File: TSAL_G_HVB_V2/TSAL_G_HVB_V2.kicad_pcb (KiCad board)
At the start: 2 copper layers, 100 x 50 mm, 48 parts, among them J1 Conn_01x03_Pin, J2 Conn_01x02_Pin, J3 Conn_01x02_Pin, J4 Conn_01x02_Pin, Q1 2N7002, Q2 MMBT3904, Q3 PMOS, U1 uA7805, U2 74HC86, U3 74AHC04, U4 74LS09, U5 NE555D

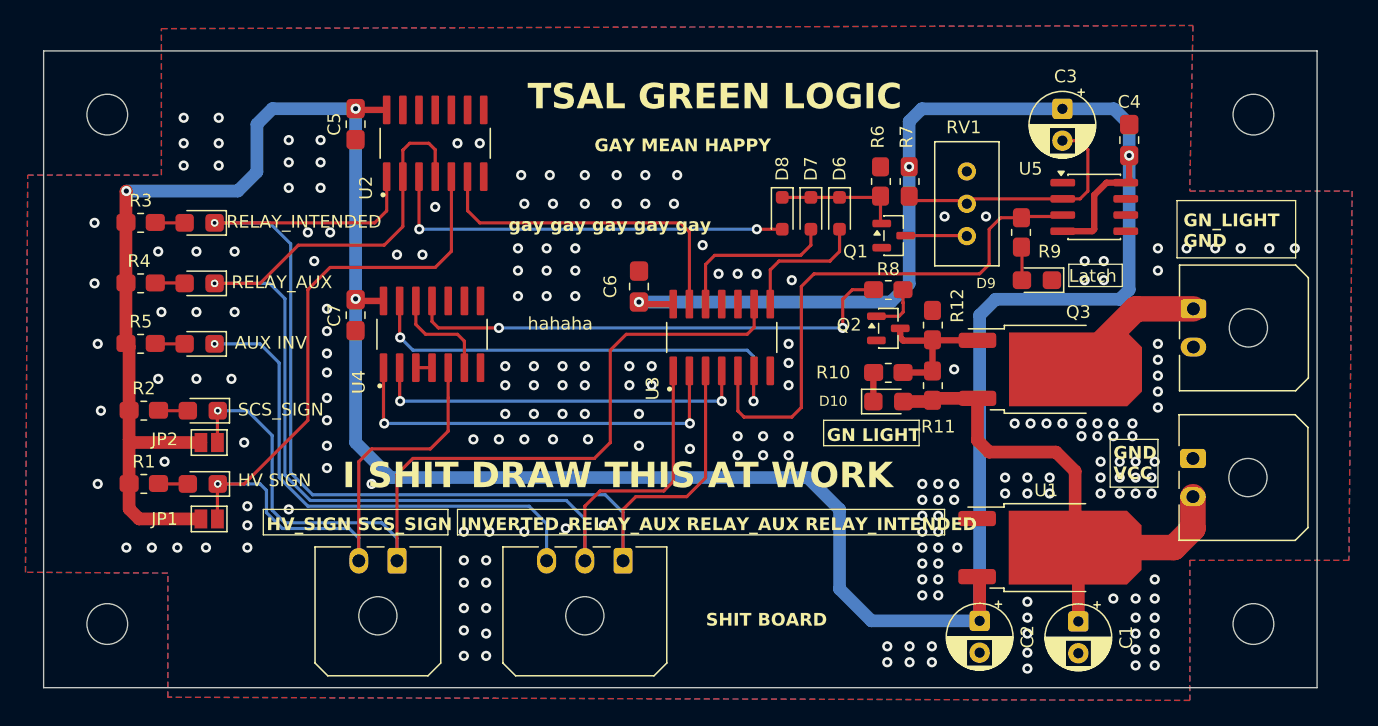
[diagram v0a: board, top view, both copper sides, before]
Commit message: TSAL GREEN SYSTEM V2 READY TO FAB
SCH&PCB updated for both HVB V2 and ACCUM V2

PCB is 9 draw at work btw
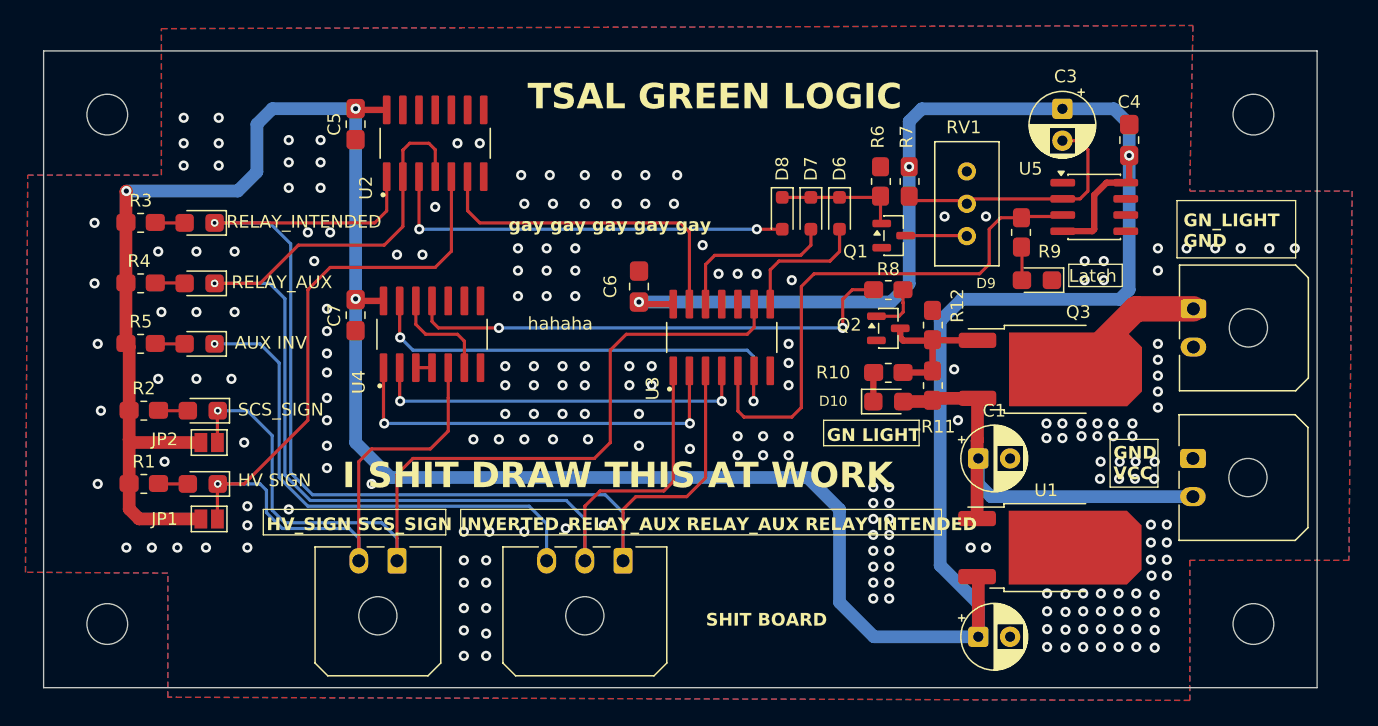
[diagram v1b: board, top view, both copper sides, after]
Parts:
- moved C1 15.0 mm to (163.4, 101.0), turned to 0 degrees
- moved C2 1.25 mm to (163.4, 115.0), turned to 0 degrees
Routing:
- net +5V: track 268.1 -> 275.6 mm
- net VCC: track 42.2 -> 34.6 mm
- net GND: track 0.00 -> 0.35 mm, vias 218 -> 221
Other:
- board text added: "SYMMETRICAL AWD"
- board text removed: "GAY MEAN HAPPY"
- board text removed: "SYMMETRICAL AWD IS BETTER THEN VTEC"

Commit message: ACCUM BOARDs BATCH ORDER
ts indicator
imd latch v2
tsalg accum v2.1
tsalg hvb v2.1
batch order
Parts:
- added D11: LED, RMC_LED:LED_0805_2012Metric_Pad1.45x1.40mm_HandSolder, F.Cu at (143.3, 71.6)
- added D12: LED, RMC_LED:LED_0805_2012Metric_Pad1.45x1.40mm_HandSolder, F.Cu at (143.3, 73.9)
- added D13: LED, RMC_LED:LED_0805_2012Metric_Pad1.45x1.40mm_HandSolder, F.Cu at (143.3, 76.2)
- added R13: 1k, RMC_Resistor:R_0805_2012Metric_Pad1.20x1.40mm_HandSolder_L, F.Cu at (138.7, 71.6)
- added R14: 1k, RMC_Resistor:R_0805_2012Metric_Pad1.20x1.40mm_HandSolder_L, F.Cu at (138.7, 73.9)
- added R15: 1k, RMC_Resistor:R_0805_2012Metric_Pad1.20x1.40mm_HandSolder_L, F.Cu at (138.7, 76.2)
- turned D1 to 0 degrees
- turned D2 to 0 degrees
- turned D3 to 0 degrees
- turned D4 to 0 degrees
- turned D5 to 0 degrees
- turned R1 to 180 degrees
- turned R2 to 180 degrees
- turned R3 to 180 degrees
- turned R4 to 180 degrees
- turned R5 to 180 degrees
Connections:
- D1 pad 1: HV_SIGN_IN -> Net-(D1-K)
- D1 pad 2: Net-(D1-A) -> HV_SIGN_IN
- D2 pad 1: SCS_SIGN_IN -> Net-(D2-K)
- D2 pad 2: Net-(D2-A) -> SCS_SIGN_IN
- D3 pad 1: RELAY_INTENDED_STATE -> Net-(D3-K)
- D3 pad 2: Net-(D3-A) -> RELAY_INTENDED_STATE
- D4 pad 1: RELAY_AUX_STATE -> Net-(D4-K)
- D4 pad 2: Net-(D4-A) -> RELAY_AUX_STATE
- D5 pad 1: INVERTED_RELAY_AUX_STATE -> Net-(D5-K)
- D5 pad 2: Net-(D5-A) -> INVERTED_RELAY_AUX_STATE
- R1 pad 1: +5V -> Net-(D1-K)
- R1 pad 2: Net-(D1-A) -> GND
- R2 pad 1: +5V -> Net-(D2-K)
- R2 pad 2: Net-(D2-A) -> GND
- R3 pad 1: +5V -> Net-(D3-K)
- R3 pad 2: Net-(D3-A) -> GND
- R4 pad 1: +5V -> Net-(D4-K)
- R4 pad 2: Net-(D4-A) -> GND
- R5 pad 1: +5V -> Net-(D5-K)
- R5 pad 2: Net-(D5-A) -> GND
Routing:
- net SCS_FAULT: track 10.5 -> 31.3 mm, vias 0 -> 2
- net TS_VOLTAGE_MISMATCH_FAULT: track 13.3 -> 28.9 mm, vias 0 -> 2
- net +5V: track 275.6 -> 263.7 mm, vias 6 -> 7
- net RELAY_PLAUSIBILITY _FAULT: track 32.6 -> 40.7 mm
- net Net-(D5-K): track 0.00 -> 2.32 mm
- net Net-(D5-A): track 2.32 -> 0.00 mm
- net Net-(D4-K): track 0.00 -> 2.32 mm
- net Net-(D4-A): track 2.32 -> 0.00 mm
- net Net-(D3-K): track 0.00 -> 2.32 mm
- net Net-(D3-A): track 2.32 -> 0.00 mm
- net Net-(D2-K): track 0.00 -> 2.32 mm
- net Net-(D2-A): track 2.32 -> 0.00 mm
- net Net-(D1-K): track 0.00 -> 2.32 mm
- net Net-(D1-A): track 2.32 -> 0.00 mm
- net Net-(D13-K): track 0.00 -> 2.28 mm
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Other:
- board text added: "2.1"
- board text added: "ALTO WORKS IS 670KG"
- board text added: "AYA"
- board text added: "GN_LIGHT = (GS * ~LS) GS=~AUX & ~INT & HV LS = (AUX^INT)|~(AUX^HV) | ~SCS HV: <60=1 AUX&INT:RELAY CLOSED=1"
- board text added: "HV_MISMATCH"
- board text added: "RELAY_PLAUS"
- board text added: "SCS_FAULT"
- board text removed: "SYMMETRICAL AWD"
- board text removed: "TSAL GREEN LOGIC GAY BOARD"
